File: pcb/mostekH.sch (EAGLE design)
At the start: 27 parts, among them Q1 BSS123, Q2 BSS123, Q3 BSS84, Q4 BSS84, T1 BC547, T2 BC547

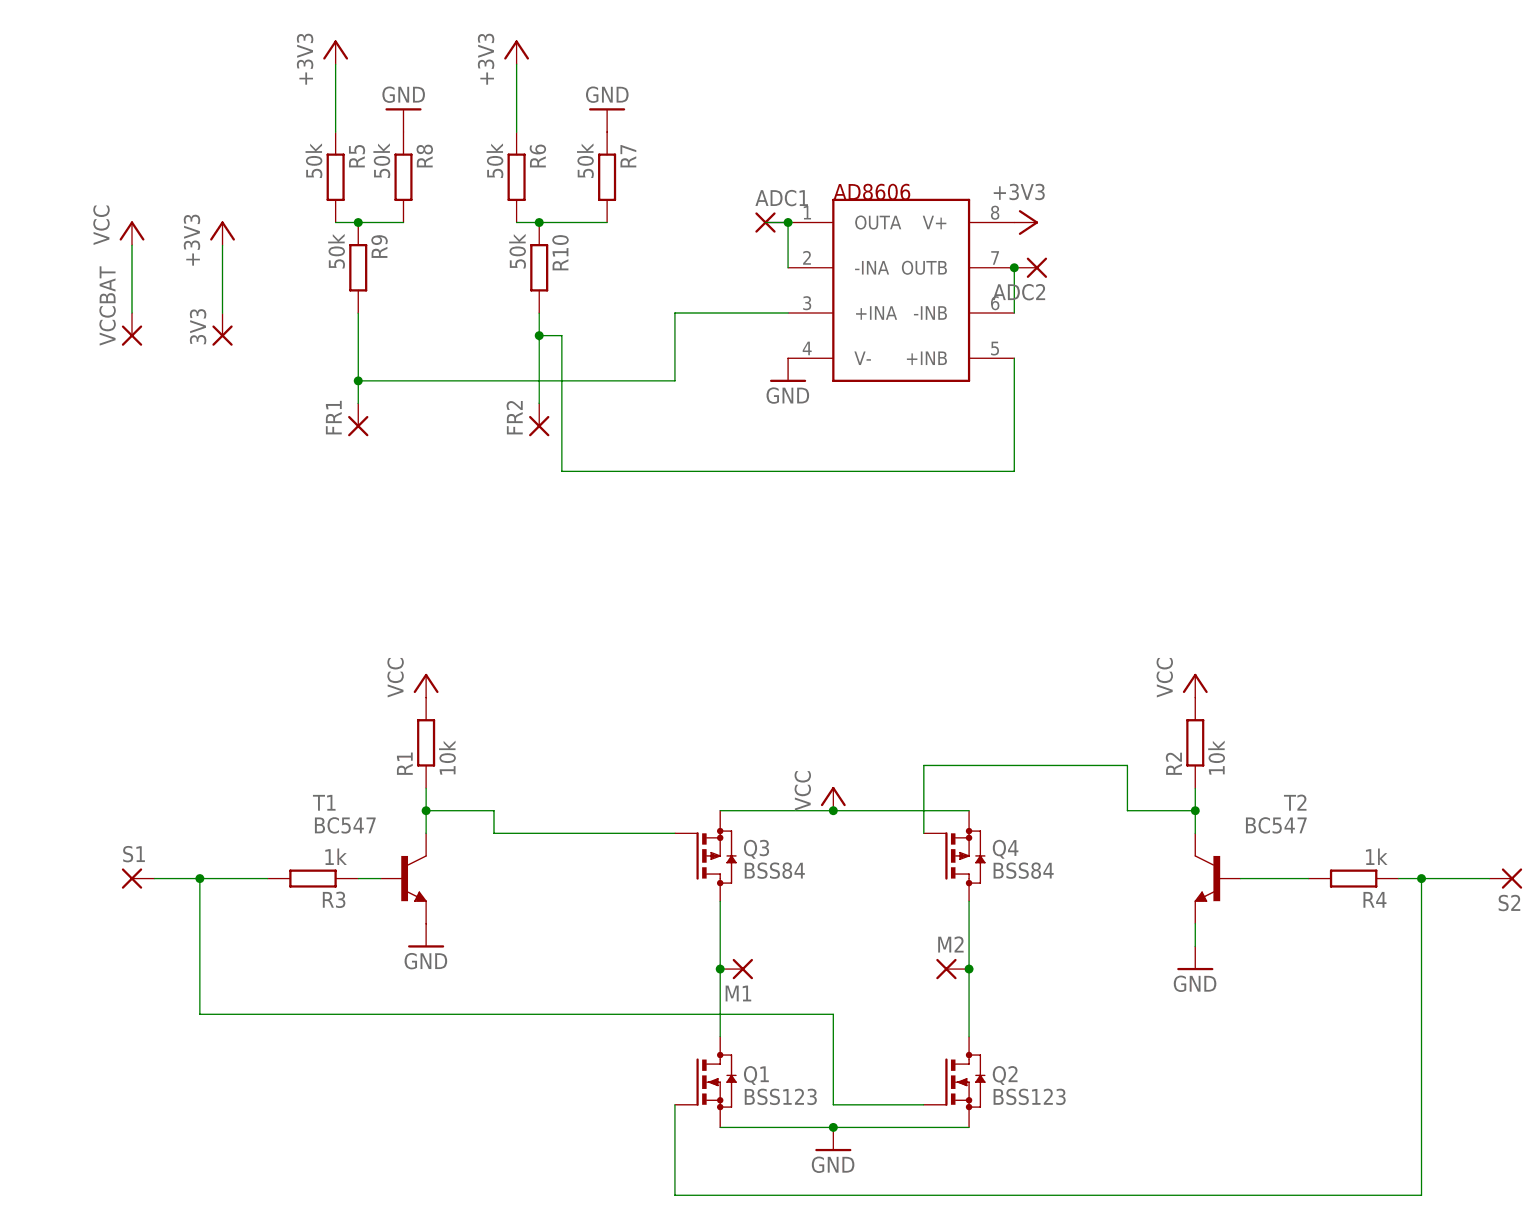
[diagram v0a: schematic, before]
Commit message: postęp w mgr.doc, aktualizacja brd mostek H, GPS dev board
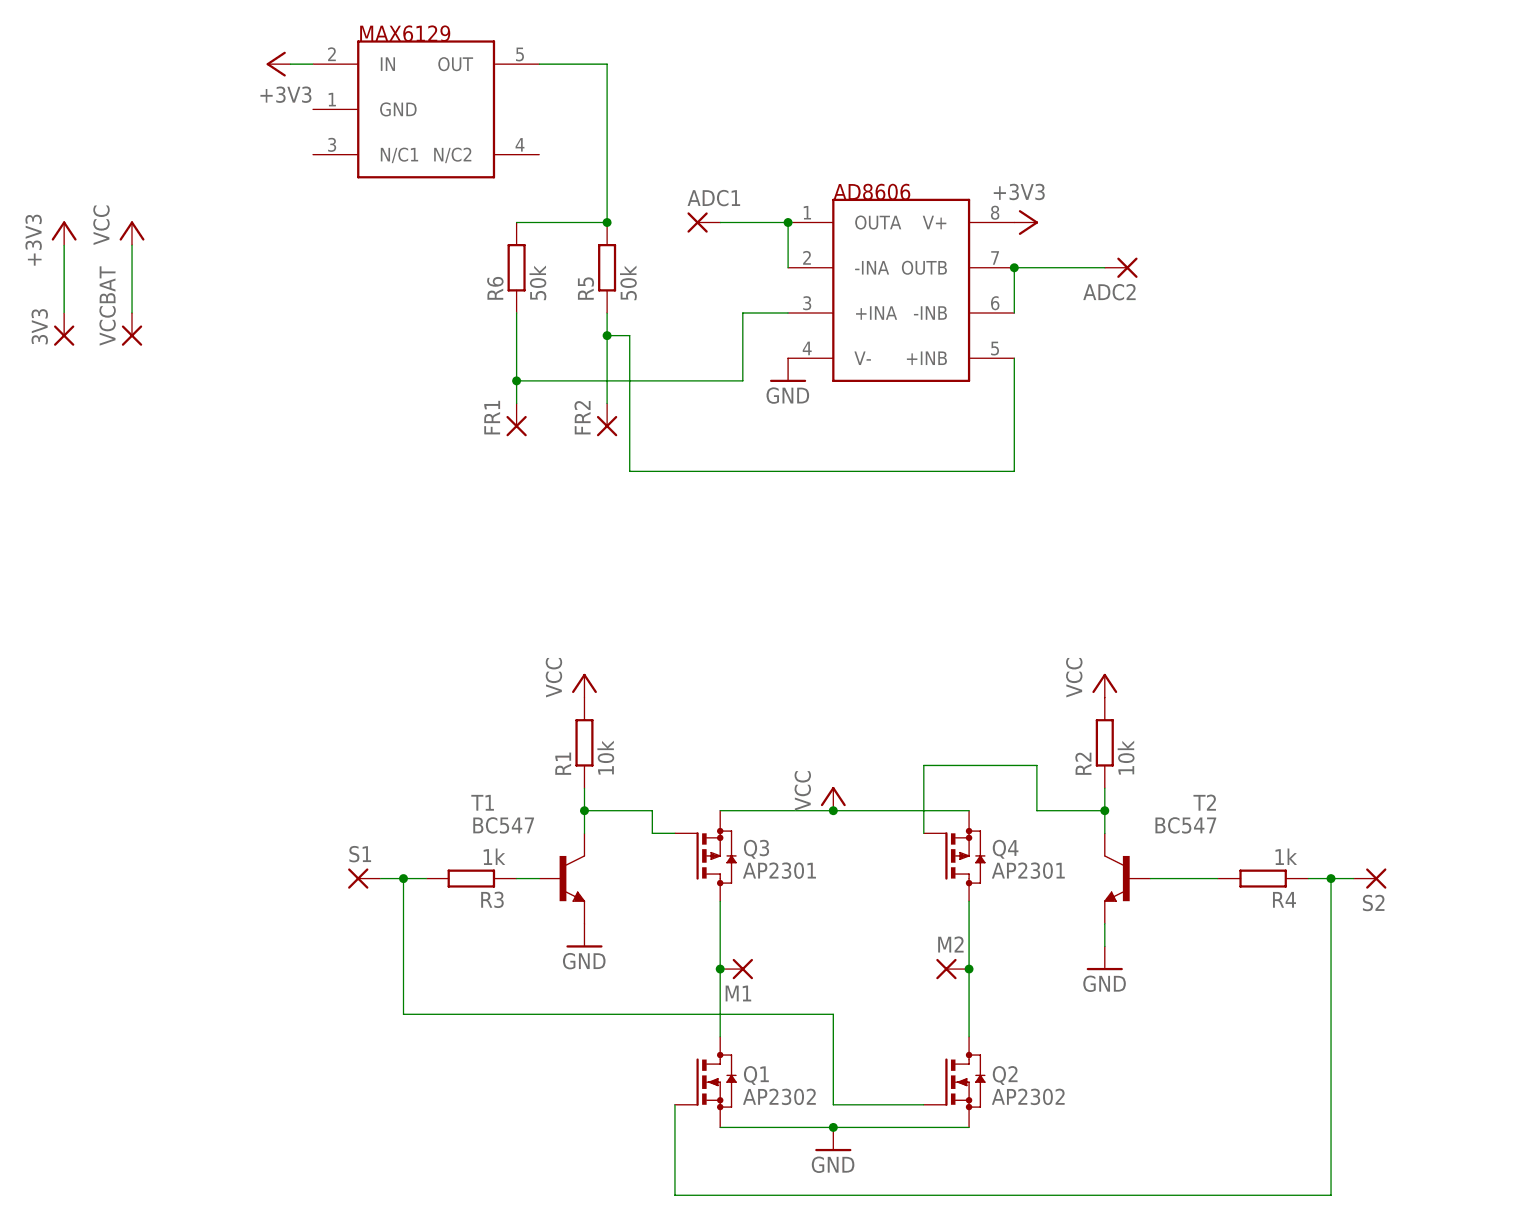
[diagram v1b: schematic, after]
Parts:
- removed R10, R7, R8, R9: 50k, rcl:R-EU_M0805
- added U$2: MAX6129, ref-packages:MAX6129
- Q1, Q2: value BSS123 -> AP2302
- Q3, Q4: value BSS84 -> AP2301
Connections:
- removed net N$14: R10.1, R6.2, R7.2
- net +3V3: now also U$2.IN; no longer R5.1, R6.1
- net GND: no longer R7.1, R8.1
- net N$13: now also R6.2, U$2.OUT; no longer R8.2, R9.1
- net N$6: now also R6.1; no longer R9.2
- net N$8: now also R5.1; no longer R10.2
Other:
- moved on the sheet: 3V3, ADC1, ADC2, FR1, FR2, R1, R2, R3, R4, R5, R6, S1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
